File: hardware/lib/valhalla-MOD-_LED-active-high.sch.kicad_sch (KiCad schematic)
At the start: 3 parts, among them U2 74LS06

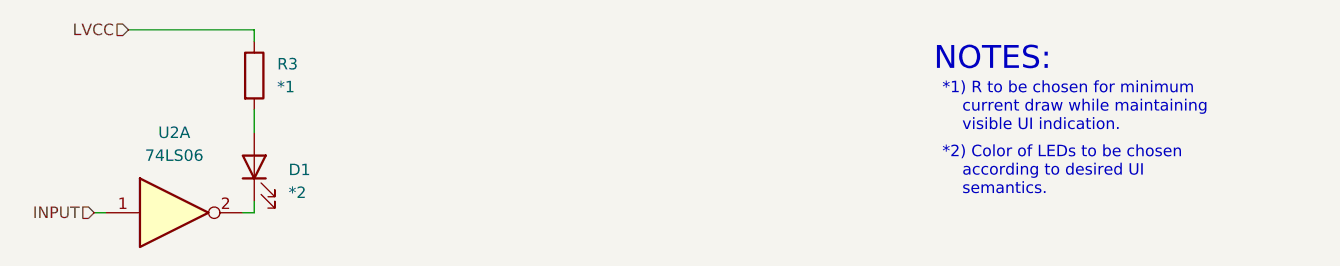
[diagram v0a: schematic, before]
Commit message: ADD: Valhalla-MOD XVR(RS485)
  - started work on the UART to RS-485 transceiver module, got stuck on
    finding a part that can either work on both 5 and 3.3V OR that has
    5V-tolerant inputs.
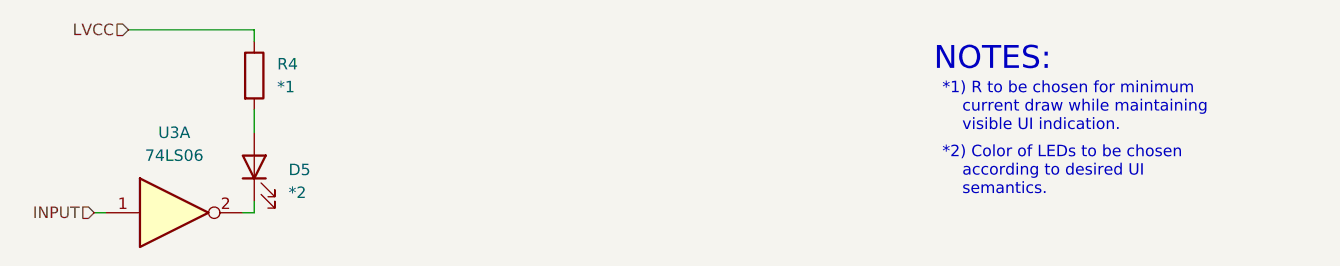
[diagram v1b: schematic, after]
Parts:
- renumbered D1 to D5, R3 to R4, U2 to U3
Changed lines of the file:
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@@
 		(dnp no)
 		(fields_autoplaced yes)
-		(property "Reference" "D1"
+		(property "Reference" "D5"
 			(at 71.12 63.8174 90)
 			(effects
@@
 		(instances
 			(project "valhalla-MOD-CPU_ATMEGA"
-				(path "/f06f94c1-3b85-417f-a10f-1ec163aec97d/80666bd4-e119-4742-84bb-076a3b6e96d5"
-					(reference "D1")
-					(unit 1)
-				)
-				(path "/f06f94c1-3b85-417f-a10f-1ec163aec97d/ea92483d-f022-41b6-a7f4-0813633f064b"
-					(reference "D2")
+				(path "/f06f94c1-3b85-417f-a10f-1ec163aec97d/4ff94fd9-b0e9-479c-b0ba-2f2eec27798f"
+					(reference "D5")
+					(unit 1)
+				)
+				(path "/f06f94c1-3b85-417f-a10f-1ec163aec97d/ccaf4ce2-d41c-402c-acb9-518abcc6cb9b"
+					(reference "D6")
 					(unit 1)
 				)
@@
 		(dnp no)
 		(fields_autoplaced yes)
-		(property "Reference" "U2"
+		(property "Reference" "U3"
 			(at 58.42 59.69 0)
 			(effects
@@
 		(instances
 			(project ""
-				(path "/f06f94c1-3b85-417f-a10f-1ec163aec97d/80666bd4-e119-4742-84bb-076a3b6e96d5"
-					(reference "U2")
-					(unit 1)
-				)
-				(path "/f06f94c1-3b85-417f-a10f-1ec163aec97d/ea92483d-f022-41b6-a7f4-0813633f064b"
-					(reference "U2")
+				(path "/f06f94c1-3b85-417f-a10f-1ec163aec97d/4ff94fd9-b0e9-479c-b0ba-2f2eec27798f"
+					(reference "U3")
+					(unit 1)
+				)
+				(path "/f06f94c1-3b85-417f-a10f-1ec163aec97d/ccaf4ce2-d41c-402c-acb9-518abcc6cb9b"
+					(reference "U3")
 					(unit 2)
 				)
@@
 		(dnp no)
 		(fields_autoplaced yes)
-		(property "Reference" "R3"
+		(property "Reference" "R4"
 			(at 69.85 52.0699 0)
 			(effects
@@
 		(instances
 			(project "valhalla-MOD-CPU_ATMEGA"
-				(path "/f06f94c1-3b85-417f-a10f-1ec163aec97d/80666bd4-e119-4742-84bb-076a3b6e96d5"
-					(reference "R3")
-					(unit 1)
-				)
-				(path "/f06f94c1-3b85-417f-a10f-1ec163aec97d/ea92483d-f022-41b6-a7f4-0813633f064b"
+				(path "/f06f94c1-3b85-417f-a10f-1ec163aec97d/4ff94fd9-b0e9-479c-b0ba-2f2eec27798f"
 					(reference "R4")
 					(unit 1)
 				)
+				(path "/f06f94c1-3b85-417f-a10f-1ec163aec97d/ccaf4ce2-d41c-402c-acb9-518abcc6cb9b"
+					(reference "R5")
+					(unit 1)
+				)
